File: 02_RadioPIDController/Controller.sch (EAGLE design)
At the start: 18 parts, among them IC1 7805TV, M1 ARDUINO-NANO-3.0, X5 236-403, X6 236-403, X7 MSTBA2

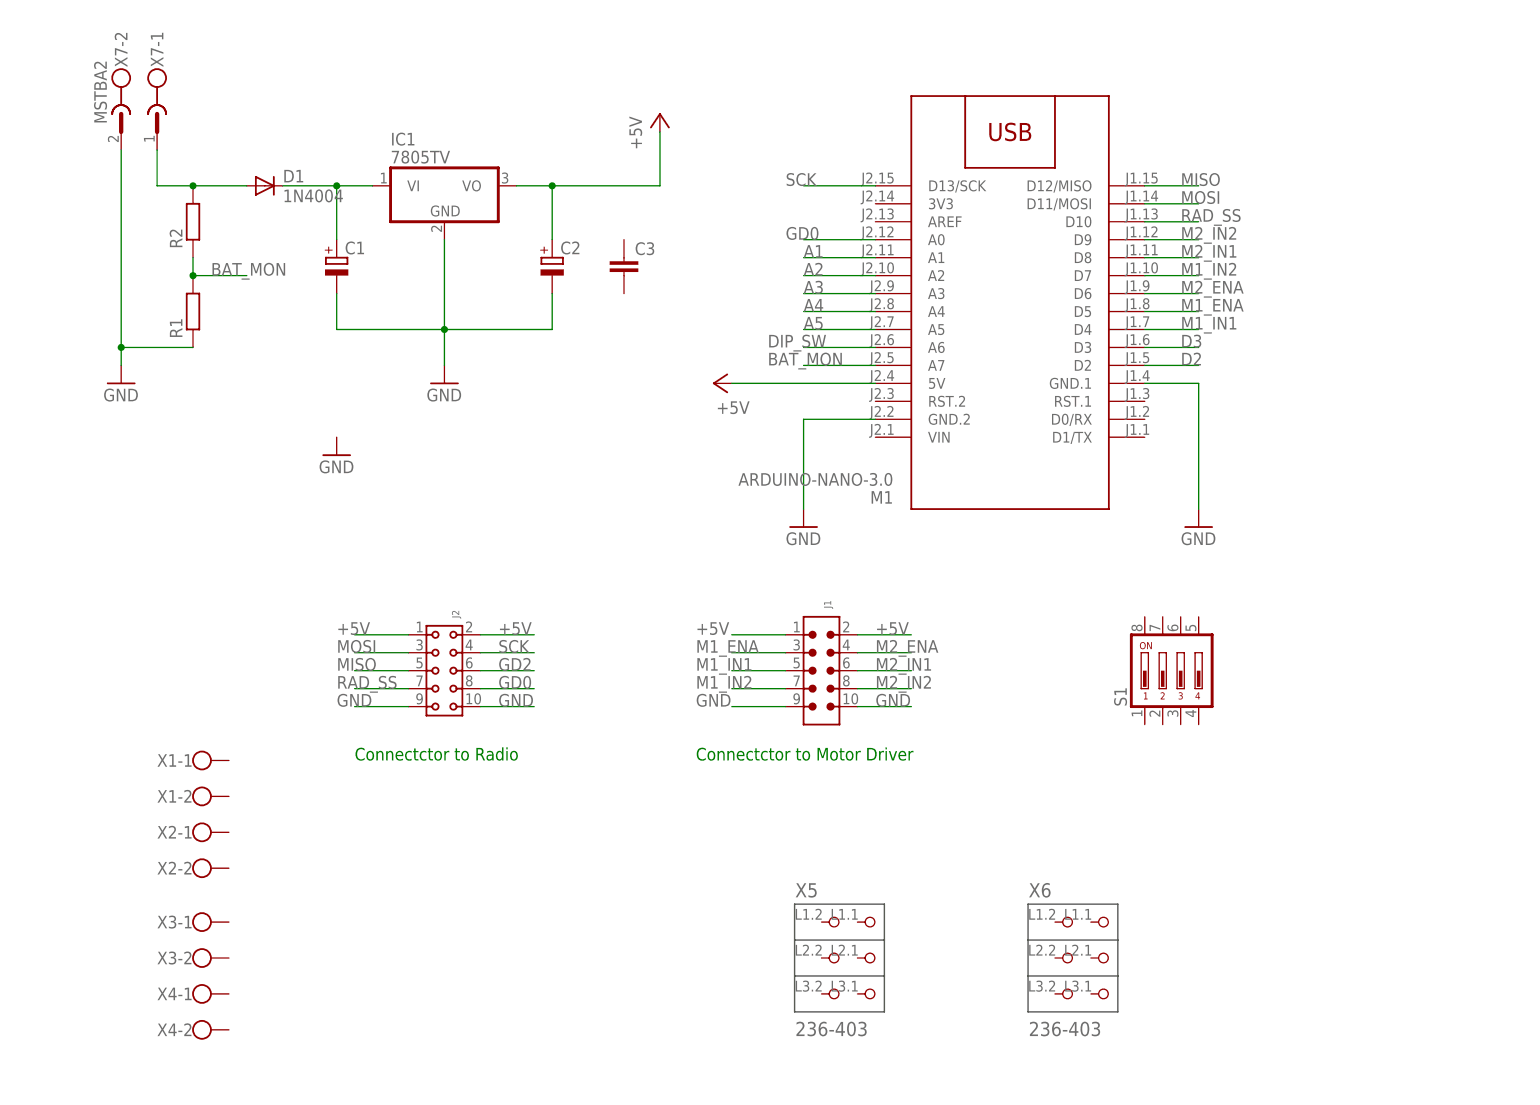
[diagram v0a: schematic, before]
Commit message: Doc for radio and controller 2
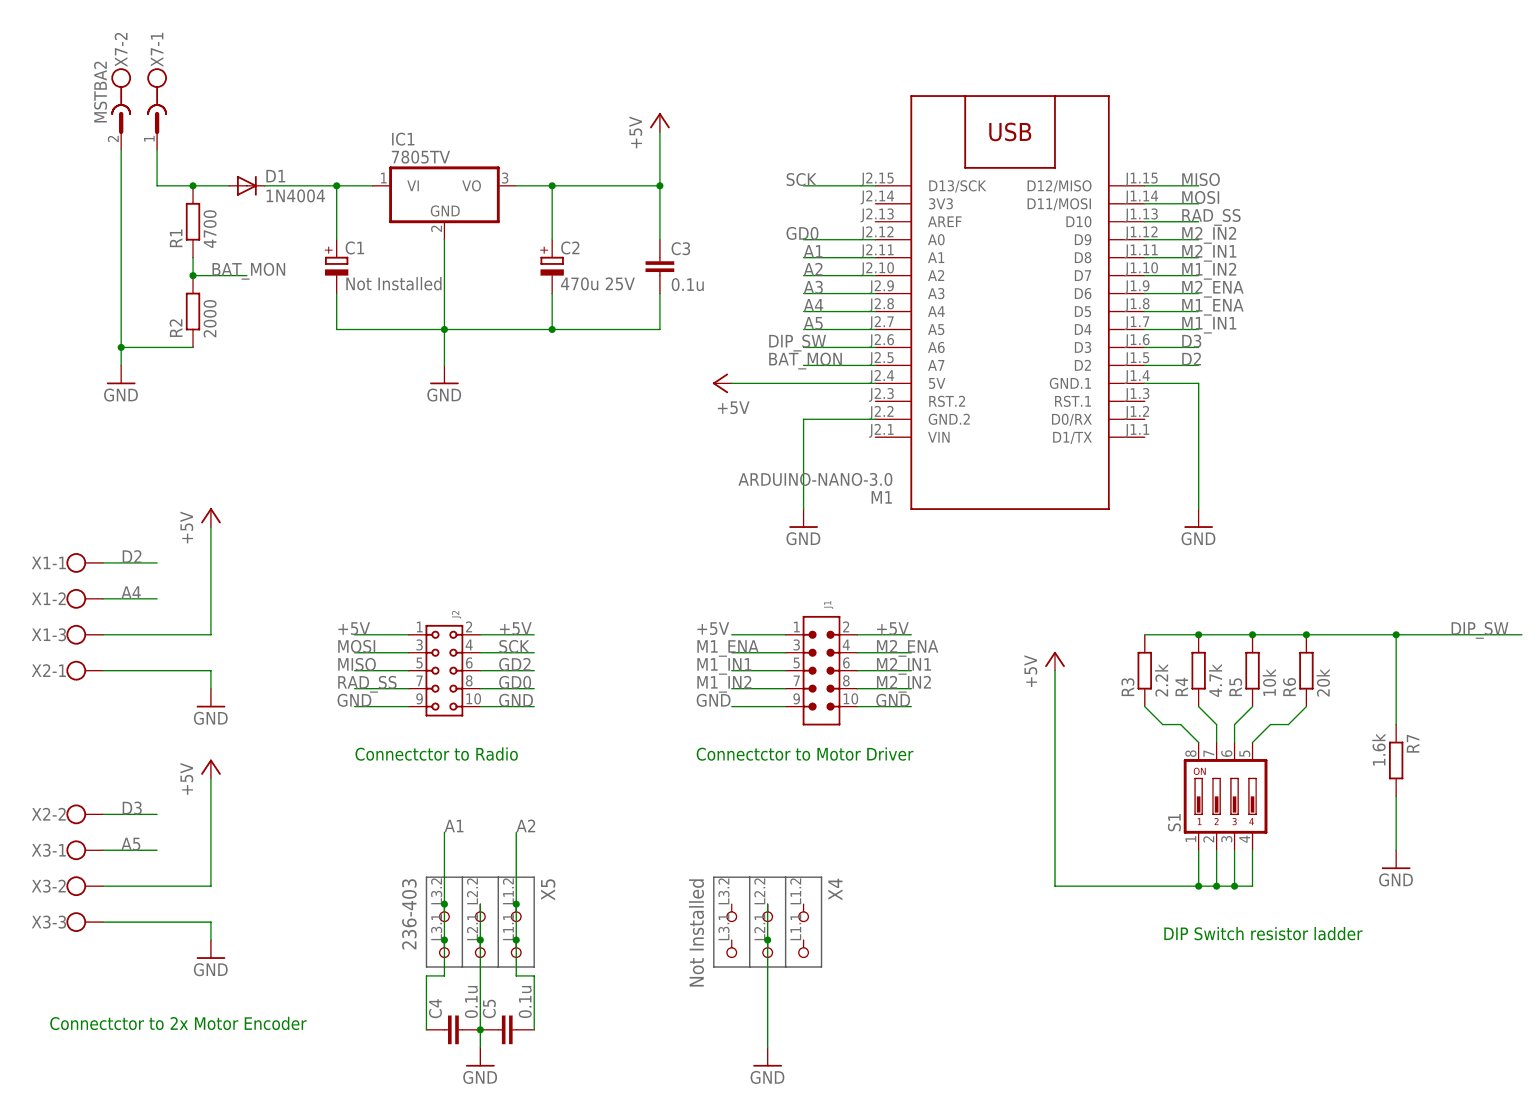
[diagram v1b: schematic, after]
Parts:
- removed X6: 236-403, con-wago_236:236-403
- added C4, C5: 0.1u, rcl:C-EU050-030X075
- added R3: 2.2k, resistor:R-EU_0207/5V
- added R4: 4.7k, resistor:R-EU_0207/5V
- added R5: 10k, resistor:R-EU_0207/5V
- added R6: 20k, resistor:R-EU_0207/5V
- added R7: 1.6k, resistor:R-EU_0207/5V
- C1: value (none) -> Not Installed
- C2: value (none) -> 470u 25V
- C3: value (none) -> 0.1u
- R1: value (none) -> 4700; device resistor:R-EU_0207/7 -> resistor:R-EU_0207/12
- R2: value (none) -> 2000
- X1, X3: device con-wago-500:W237-102 -> con-wago-500:W237-103
- X4: value (none) -> Not Installed; device con-wago-500:W237-102 -> con-wago_236:236-403
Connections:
- new net N$4: R4.1, S1.7
- new net N$5: R5.1, S1.6
- new net N$6: R6.1, S1.5
- new net N$7: R3.1, S1.8
- net +5V: now also C3.1, S1.1, S1.2, S1.3, S1.4, X1-3.KL, X3-2.KL
- net A1: now also C4.1, X5.P3.1, X5.P3.2
- net A2: now also C5.2, X5.P1.1, X5.P1.2
- net A4: now also X1-2.KL
- net A5: now also X3-1.KL
- net BAT_MON: now also R1.1, R2.2; no longer R1.2, R2.1
- net D2: now also X1-1.KL
- net D3: now also X2-2.KL
- net DIP_SW: now also R3.2, R4.2, R5.2, R6.2, R7.1
- net GND: now also C3.2, C4.2, C5.1, R2.1, R7.2, X2-1.KL, X3-3.KL, X4.P2.1, X4.P2.2, X5.P2.1, X5.P2.2; no longer R1.1
- net N$1: now also R1.2; no longer R2.2
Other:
- note added: "Connectctor to 2x Motor Encoder"
- note added: "DIP Switch resistor ladder"
- moved on the sheet: C3, D1, R1, R2, S1, X1-1, X1-2, X2-1, X2-2, X3-1, X3-2, X5
